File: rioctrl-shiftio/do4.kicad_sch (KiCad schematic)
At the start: 2 parts, among them U6 ELQ3H4

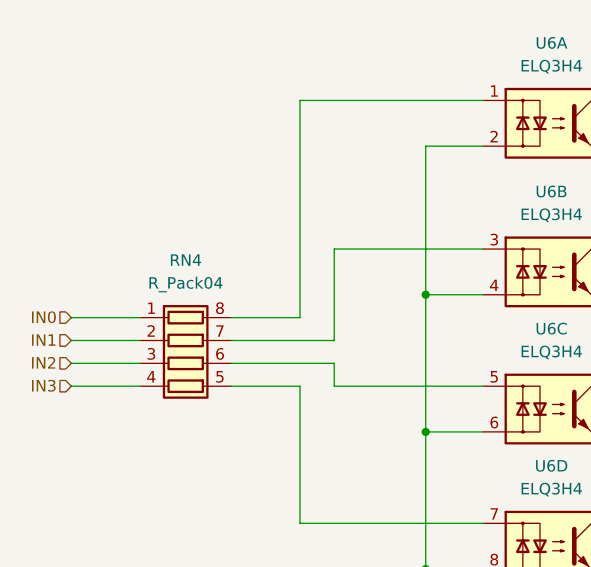
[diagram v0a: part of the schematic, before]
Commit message: Fill in BOM (LCSC#)
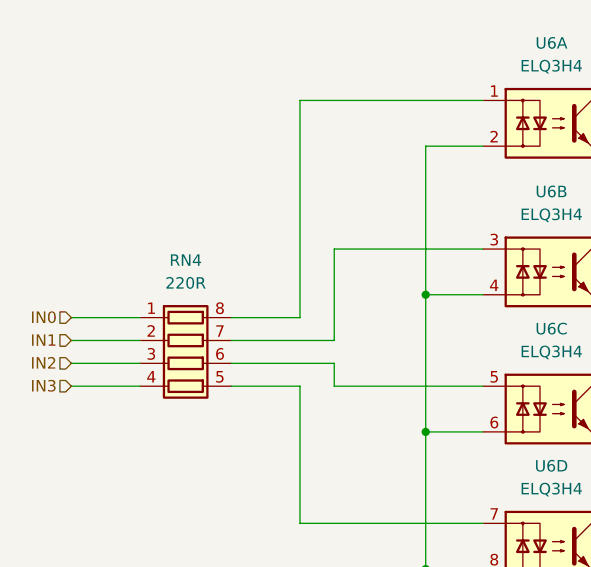
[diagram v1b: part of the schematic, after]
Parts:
- RN4: value R_Pack04 -> 220R; LCSC# (none) -> C706474
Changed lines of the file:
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@@
 			)
 		)
-		(property "Value" "R_Pack04"
+		(property "Value" "220R"
 			(at 83.82 68.58 90)
 			(effects
@@
 			(at 83.82 77.47 0)
 			(effects
+				(font
+					(size 1.27 1.27)
+				)
+				(hide yes)
+			)
+		)
+		(property "LCSC#" "C706474"
+			(at 83.82 77.47 0)
+			(effects
